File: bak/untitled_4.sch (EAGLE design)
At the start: 99 parts, among them IC1 LM1875T, IC2 LM1875T, IC3 LM1875T, IC4 LM1875T, IC5 NE5532N, IC6 NE5532N, J2 power, J3 audio_output, J4 B3P-VH(LF)(SN), J5 +25v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

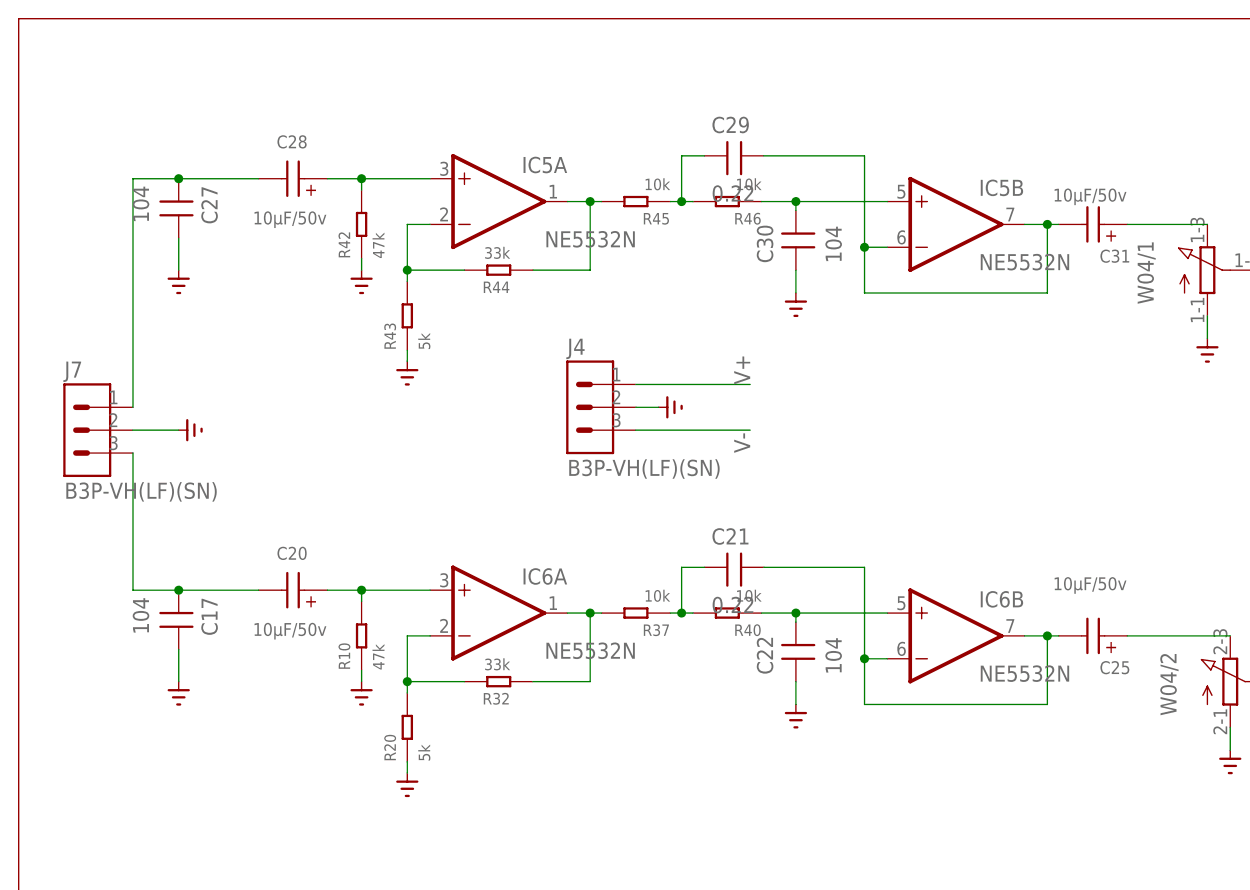
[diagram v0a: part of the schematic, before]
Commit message: 后级放大:更新
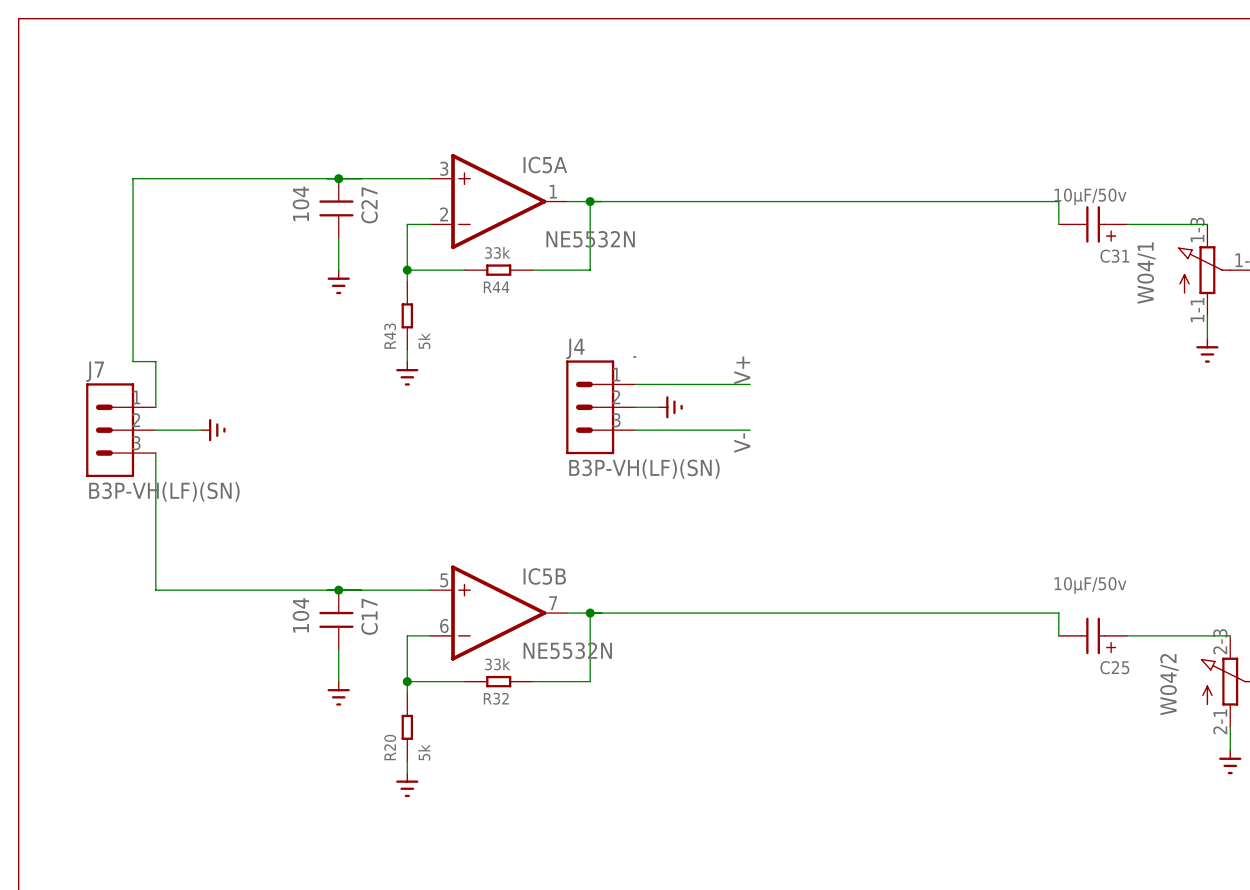
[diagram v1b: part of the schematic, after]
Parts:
- removed C20, C28: 10µF/50v, Wurth_Capacitors_WCAP-AT1H:WCAP-AT1H_5X11_860240272001
- removed C21, C29: 0.22, Audio-Power-amlifier:5.08MM-
- removed C22, C30: 104, Audio-Power-amlifier:5.08MM-
- removed IC6: NE5532N, linear:NE5532N
- removed R10, R42: 47k, OPL_Resistor:DIP-RES-1M-5%-1/4W(PR-D2.3XL6.5MM)
- removed R37, R40, R45, R46: 10k, OPL_Resistor:DIP-RES-1M-5%-1/4W(PR-D2.3XL6.5MM)
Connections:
- removed net N$27: C20.+, IC6A.+IN, R10.2
- removed net N$49: C28.+, IC5A.+IN, R42.2
- removed net N$59: C21.1, R37.1, R40.2
- removed net N$60: C22.2, IC6B.+IN, R40.1
- removed net N$61: C21.2, C25.-, IC6B.-IN, IC6B.OUT
- removed net N$62: C29.2, C31.-, IC5B.-IN, IC5B.OUT
- removed net N$65: C29.1, R45.1, R46.2
- removed net N$66: C30.2, IC5B.+IN, R46.1
- net GND: no longer C22.1, C30.1, R10.1, R42.1
- net N$13: now also IC5B.+IN; no longer C20.-
- net N$16: now also IC5A.+IN; no longer C28.-
- net N$39: now also IC5B.-IN; no longer IC6A.-IN
- net N$55: now also C25.-, IC5B.OUT; no longer IC6A.OUT, R37.2
- net N$64: now also C31.-; no longer R45.2
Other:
- moved on the sheet: C17, C27, IC5B, J7
